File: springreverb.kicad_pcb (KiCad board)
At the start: 2 copper layers, 42 parts, among them J1 IN, J11 From2, J12 From, J13 VR2_3, J2 GND2, J3 GND, J4 Vin, J5 VR1_3, J6 VR1_2, J7 To, J8 To2, U1 TL072, U2 TC1044S, U3 4556ADD

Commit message: 配置修整
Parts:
- added R14: 10, Resistor_THT:R_Axial_DIN0204_L3.6mm_D1.6mm_P7.62mm_Horizontal, F.Cu at (118.4, 168.3)
- added R15: 10, Resistor_THT:R_Axial_DIN0204_L3.6mm_D1.6mm_P7.62mm_Horizontal, F.Cu at (115.3, 168.4)
- J2: value GND2 -> VR1_1
- R10: value 10 -> 47
- R12: footprint Resistor_THT:R_Axial_DIN0204_L3.6mm_D1.6mm_P7.62mm_Horizontal -> Resistor_THT:R_Axial_DIN0204_L3.6mm_D1.6mm_P2.54mm_Vertical
- R7: value 10 -> 100
- moved J2 80.0 mm to (128.4, 157.4), turned to 0 degrees
- moved J7 60.2 mm to (112.3, 168.1)
- moved R10 57.5 mm to (110.4, 144.3), turned to 0 degrees
- moved C8 51.6 mm to (121.2, 157.2)
- moved J1 49.5 mm to (117.9, 87.8), turned to 90 degrees
- moved C18 48.3 mm to (121.5, 149.2), turned to 90 degrees
- moved R1 47.2 mm to (117.8, 91.7), turned to -90 degrees
- moved U3 46.8 mm to (118.0, 156.3)
- moved C17 46.8 mm to (109.9, 161.2)
- moved C16 46.7 mm to (105.3, 158.7), turned to -90 degrees
- moved R7 46.3 mm to (107.4, 155.6)
- moved C19 46.0 mm to (123.5, 141.9)
- moved J6 45.9 mm to (128.4, 148.5)
- moved R4 45.6 mm to (120.8, 151.6)
- moved R5 45.2 mm to (128.4, 154.1)
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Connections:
- J11 pad 1: GND3 -> GND
- J2 pad 1: GND2 -> Net-(J2-Pin_1)
- R11 pad 2: GND3 -> GND
- R2 pad 2: GND2 -> GND
- R5 pad 1: GND3 -> Net-(J2-Pin_1)
- U3 pad 1: Net-(J7-Pin_1) -> Net-(R14-Pad2)
- U3 pad 7: Net-(J7-Pin_1) -> Net-(R15-Pad2)
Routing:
- net GND: track 143.0 -> 87.4 mm
- net Net-(U1C-V+): track 33.8 -> 13.2 mm
- net Net-(J7-Pin_1): track 19.6 -> 0.00 mm
- net Net-(U3C-V+): track 15.0 -> 0.00 mm
- net Net-(J8-Pin_1): track 23.3 -> 8.67 mm
- net GND3: track 12.5 -> 0.00 mm
- net Net-(U3C-V-): track 15.0 -> 3.70 mm
- net Net-(U1A-+): track 9.83 -> 21.0 mm
- net Net-(U2-CAP+): track 12.9 -> 5.22 mm
- net Net-(C3-Pad1): track 18.6 -> 11.2 mm
- net Net-(C10-Pad1): track 11.4 -> 18.3 mm
- net Net-(C2-Pad1): track 9.12 -> 4.22 mm
- net GND2: track 4.57 -> 0.00 mm
- net Net-(J6-Pin_1): track 3.84 -> 0.00 mm
- net Net-(U3A-+): track 12.5 -> 8.67 mm
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
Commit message: 部品を配置した
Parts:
- removed the J7 at (112.3, 168.1)
- added H1: MountingHole, MountingHole:MountingHole_3.2mm_M3, F.Cu at (59.7, 72.4)
- added H2: MountingHole, MountingHole:MountingHole_3.2mm_M3, F.Cu at (113.0, 72.6)
- added H3: MountingHole, MountingHole:MountingHole_3.2mm_M3, F.Cu at (59.7, 115.6)
- added H4: MountingHole, MountingHole:MountingHole_3.2mm_M3, F.Cu at (113.0, 115.6)
- added J10: To2, MyLibrary:PinHeader_1x01_P2.54mm_Vertical, F.Cu at (65.2, 79.6)
- added J16: VR2_3GND, MyLibrary:PinHeader_1x01_P2.54mm_Vertical, F.Cu at (100.1, 101.3)
- added J2: INGND, MyLibrary:PinHeader_1x01_P2.54mm_Vertical, F.Cu at (111.8, 95.8)
- added J9: To, MyLibrary:PinHeader_1x01_P2.54mm_Vertical, F.Cu at (65.1, 75.1)
- C11, C14: value 25v100u -> 100u
- C3, C9: value 50v100u -> 1000u; footprint Capacitor_THT:CP_Radial_D7.5mm_P2.50mm -> Capacitor_THT:CP_Radial_D10.0mm_P5.00mm
- J13: renamed from J11; value From2 -> FromGND
- J8: value To2 -> ToGND
- moved R7 109.2 mm to (73.7, 68.6), turned to -90 degrees
- moved J6 102.5 mm to (57.9, 82.9), turned to 180 degrees
- moved R6 100.2 mm to (82.4, 73.8), turned to -90 degrees
- moved R5 97.8 mm to (61.2, 82.9), turned to 0 degrees
- moved C6 93.0 mm to (68.6, 80.5), turned to 90 degrees
- moved C16 91.5 mm to (79.8, 70.9), turned to 180 degrees
- moved C17 90.5 mm to (79.7, 75.8), turned to 180 degrees
- moved J7 90.0 mm to (61.2, 88.5), turned to 0 degrees
- moved U3 88.8 mm to (71.6, 80.7), turned to 0 degrees
- moved R4 84.2 mm to (68.9, 85.3), turned to 180 degrees
- moved C18 81.4 mm to (68.1, 87.8), turned to -90 degrees
- moved C19 74.1 mm to (67.1, 93.7), turned to -90 degrees
- moved R9 74.0 mm to (83.1, 85.7), turned to -90 degrees
- moved J8 73.8 mm to (69.5, 73.8), turned to 0 degrees
- moved C14 61.1 mm to (90.5, 78.5), turned to 180 degrees
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- renumbered C8 to C6, C6 to C7, C7 to C8, J12 to J14, J13 to J15, J2 to J6, J6 to J7, R8 to R10, R9 to R11, R10 to R12, R11 to R13, R12 to R14, R15 to R6, R14 to R7, R6 to R8, R7 to R9
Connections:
- C6 pad 1: Net-(J8-Pin_1) -> Net-(J10-Pin_1)
- J8 pad 1: Net-(J8-Pin_1) -> GND
- R5 pad 2: Net-(J8-Pin_1) -> Net-(J10-Pin_1)
- U3 pad 2: Net-(J8-Pin_1) -> Net-(J10-Pin_1)
- U3 pad 6: Net-(J8-Pin_1) -> Net-(J10-Pin_1)
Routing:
- net GND: track 87.4 -> 188.3 mm, vias 0 -> 2
- net Net-(J11-In): track 0.00 -> 30.7 mm
- net Net-(C3-Pad1): track 11.2 -> 41.4 mm
- net Net-(U3C-V+): track 0.00 -> 22.7 mm
- net Net-(J10-Pin_1): track 0.00 -> 17.9 mm
- net Net-(U3C-V-): track 3.70 -> 20.8 mm
- net Net-(U1C-V-): track 12.0 -> 27.1 mm
- net Net-(C10-Pad1): track 18.3 -> 33.2 mm
- net Net-(J8-Pin_1): track 8.67 -> 0.00 mm
- net Net-(J12-In): track 10.6 -> 3.92 mm
- net Net-(R7-Pad2): track 0.00 -> 5.26 mm
- net Net-(R6-Pad2): track 0.00 -> 4.52 mm
- net Net-(J6-Pin_1): track 0.00 -> 3.33 mm
- net Net-(J7-Pin_1): track 0.00 -> 3.18 mm
- net Net-(U3A-+): track 8.67 -> 11.6 mm
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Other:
- board outline added: 65 x 54.7 mm

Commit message: 配線のクリアランスを0.4にして修正
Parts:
- C16, C19: value 25v100u -> 100u
- C2: value 0.1 -> 0.1u
- moved C18 0.50 mm to (68.1, 88.3)
- moved C19 0.47 mm to (67.1, 94.2)
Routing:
- net GND: track 188.3 -> 189.7 mm
- net Net-(U1C-V-): track 27.1 -> 25.9 mm
- net Net-(U3C-V+): track 22.7 -> 23.5 mm
- net Net-(J15-Pin_1): track 9.63 -> 10.3 mm
- net Net-(R6-Pad2): track 4.52 -> 3.95 mm

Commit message: ボリュームのつなぎ方とか色々修正
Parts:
- removed J7: VR1_2, MyLibrary:PinHeader_1x01_P2.54mm_Vertical
- J5: value VR1_3 -> VR1_2
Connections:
- R4 pad 2: Net-(J7-Pin_1) -> Net-(J6-Pin_1)
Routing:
- net Net-(J7-Pin_1): track 3.18 -> 0.00 mm
- net Net-(J6-Pin_1): track 3.33 -> 5.75 mm

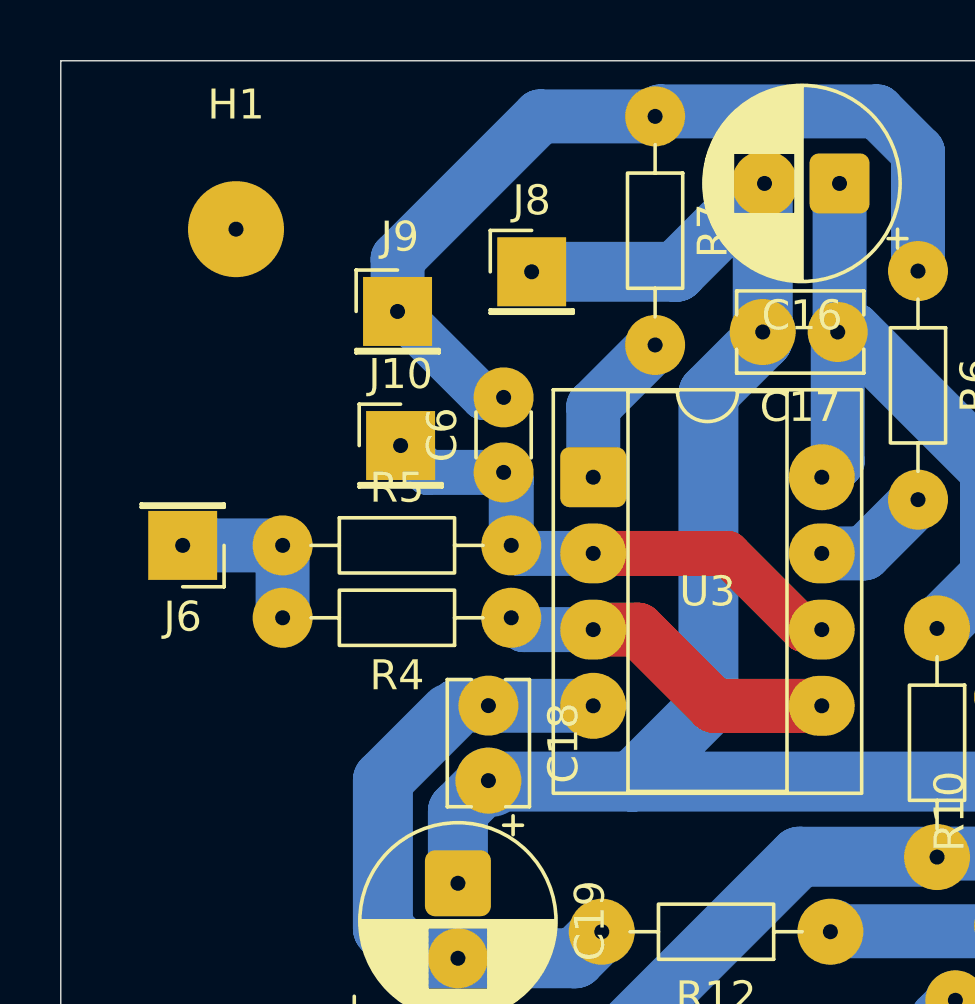
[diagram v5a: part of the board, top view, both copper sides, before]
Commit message: 発振対策とVPの接続先を修正
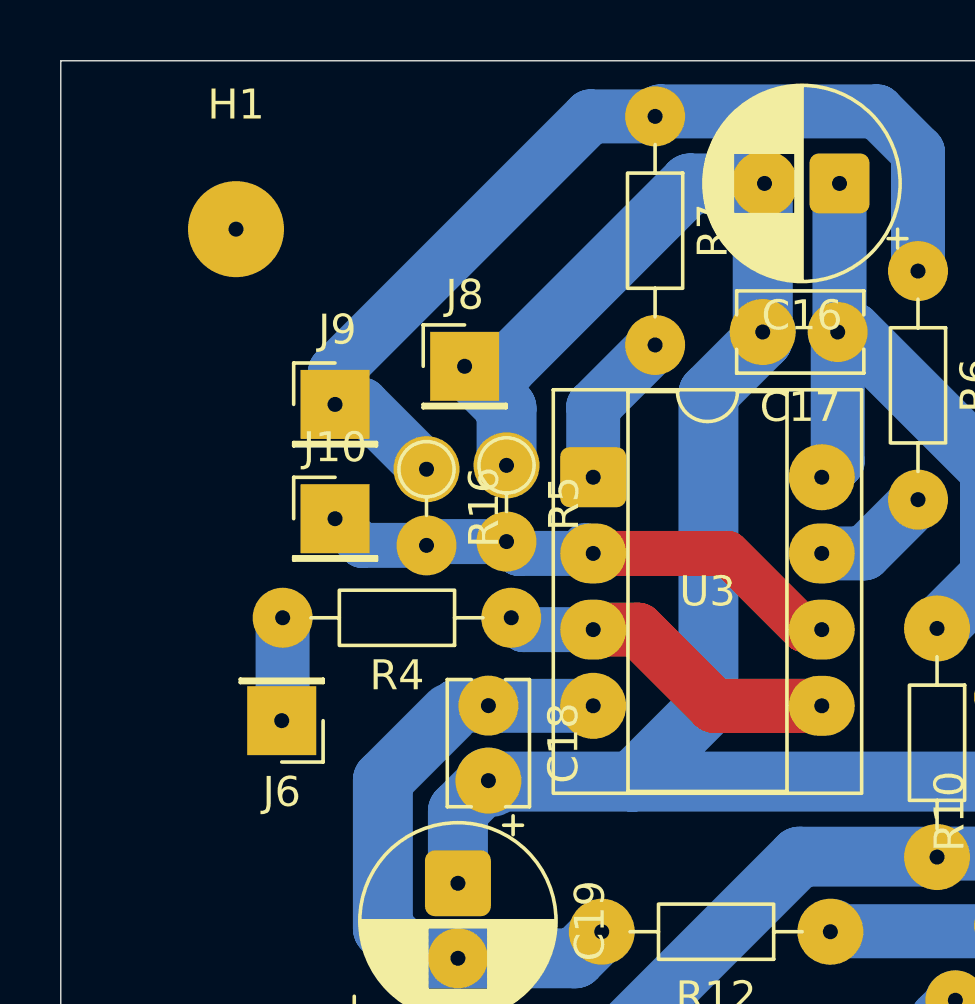
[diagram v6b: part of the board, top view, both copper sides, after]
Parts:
- removed C6: 47p, Capacitor_THT:C_Disc_D3.0mm_W1.6mm_P2.50mm
- added R16: 1k, Resistor_THT:R_Axial_DIN0204_L3.6mm_D1.6mm_P2.54mm_Vertical, F.Cu at (66.0, 80.4)
- J5: value VR1_2 -> VR1_3
- J6: value VR1_1 -> VR1_2
- R4: value 220 -> 470
- R5: footprint Resistor_THT:R_Axial_DIN0204_L3.6mm_D1.6mm_P7.62mm_Horizontal -> Resistor_THT:R_Axial_DIN0204_L3.6mm_D1.6mm_P2.54mm_Vertical
- moved R5 7.92 mm to (68.7, 80.3), turned to -90 degrees
- moved J6 6.71 mm to (61.2, 88.8)
- moved J8 3.86 mm to (67.3, 77.0)
- moved J9 3.73 mm to (63.0, 78.2)
- moved J10 3.27 mm to (63.0, 82.0)
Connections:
- R5 pad 1: Net-(J6-Pin_1) -> GND
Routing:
- net GND: track 189.7 -> 197.1 mm
- net Net-(J6-Pin_1): track 5.75 -> 3.44 mm
- net Net-(J11-In): track 30.4 -> 32.6 mm

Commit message: 増幅率やVR1とC5の前後を入れ替えたり
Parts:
- removed R4: 470, Resistor_THT:R_Axial_DIN0204_L3.6mm_D1.6mm_P7.62mm_Horizontal
- removed R6: 10, Resistor_THT:R_Axial_DIN0204_L3.6mm_D1.6mm_P7.62mm_Horizontal
- added C5: 100u, Capacitor_THT:CP_Radial_D6.3mm_P2.50mm, F.Cu at (103.5, 76.3)
- added J7: VR3_1, MyLibrary:PinHeader_1x01_P2.54mm_Vertical, F.Cu at (106.2, 69.5)
- R5: value 220 -> 1.2k
- moved J5 7.43 mm to (101.3, 69.5)
- moved J6 7.01 mm to (67.2, 85.1)
- moved J9 4.78 mm to (66.7, 75.2)
- moved J10 4.31 mm to (62.0, 77.9)
- moved J8 4.09 mm to (70.6, 74.5)
- moved R16 1.66 mm to (65.9, 78.7)
- moved R5 1.52 mm to (68.7, 78.7)
- moved R12 0.82 mm to (79.9, 96.5)
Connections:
- U1 pad 1: Net-(J5-Pin_1) -> Net-(U1A--)
- U1 pad 2: Net-(J5-Pin_1) -> Net-(U1A--)
- U3 pad 3: Net-(U3A-+) -> Net-(J6-Pin_1)
- U3 pad 5: Net-(U3A-+) -> Net-(J6-Pin_1)
- U3 pad 7: Net-(R6-Pad2) -> Net-(J11-In)
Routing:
- net Net-(U3A-+): track 11.6 -> 0.00 mm
- net Net-(J6-Pin_1): track 3.44 -> 13.4 mm
- net Net-(J11-In): track 32.6 -> 39.4 mm, vias 0 -> 2
- net Net-(U1A--): track 0.00 -> 6.48 mm
- net Net-(R6-Pad2): track 3.95 -> 0.00 mm
- net Net-(J10-Pin_1): track 18.2 -> 21.8 mm
- net GND: track 197.1 -> 194.4 mm
- net Net-(J5-Pin_1): track 6.22 -> 8.81 mm
